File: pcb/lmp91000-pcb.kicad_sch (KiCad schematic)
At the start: 28 parts, among them J1 TC2030, SW1 SW_Push, U1 EFR32BG24L210F768IM40-B, U5 2450AT18D0100001E, Y1 XTL501250-S315-038

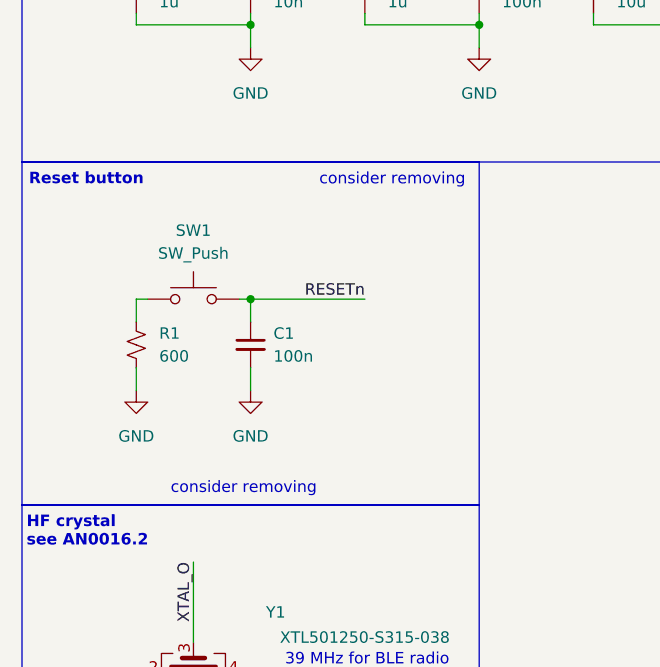
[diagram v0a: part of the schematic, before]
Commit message: Remove reset button
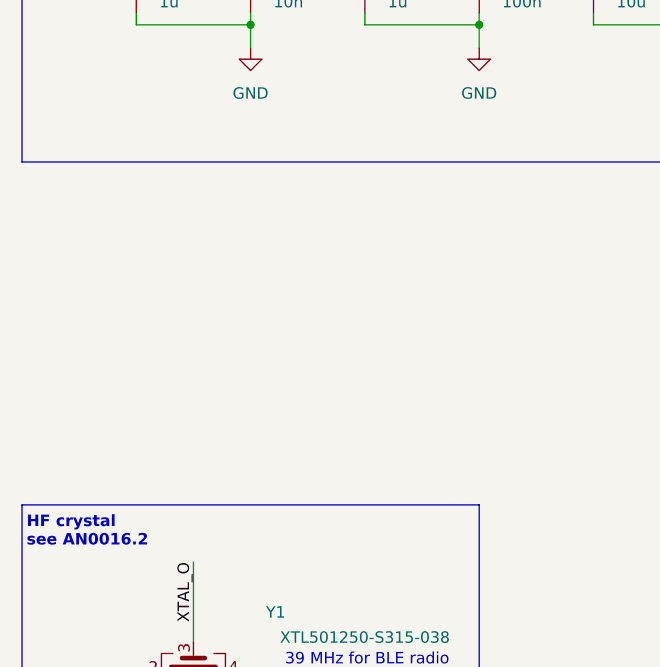
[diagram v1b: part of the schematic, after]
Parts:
- removed C1: 100n, symbol Device:C_Small
- removed R1: 600, symbol Device:R_Small_US
- removed SW1: SW_Push, symbol Switch:SW_Push
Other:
- note removed: "Reset button"
- note removed: "consider removing"

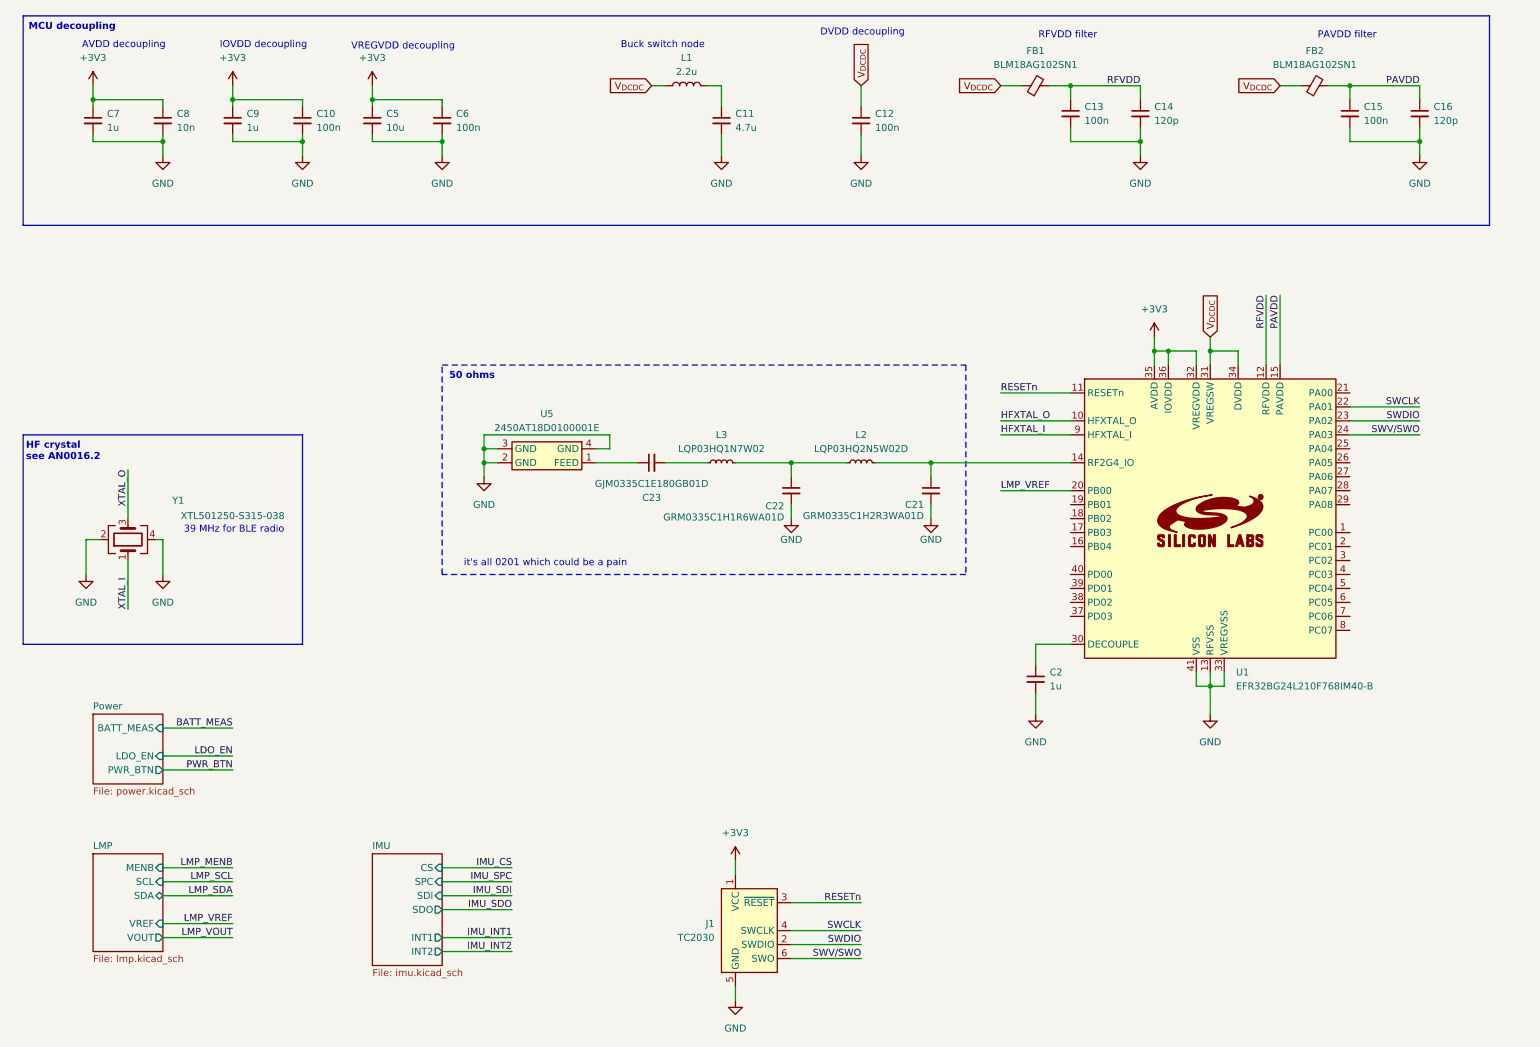
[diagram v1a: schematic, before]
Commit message: Simplify to minimum buck converter components
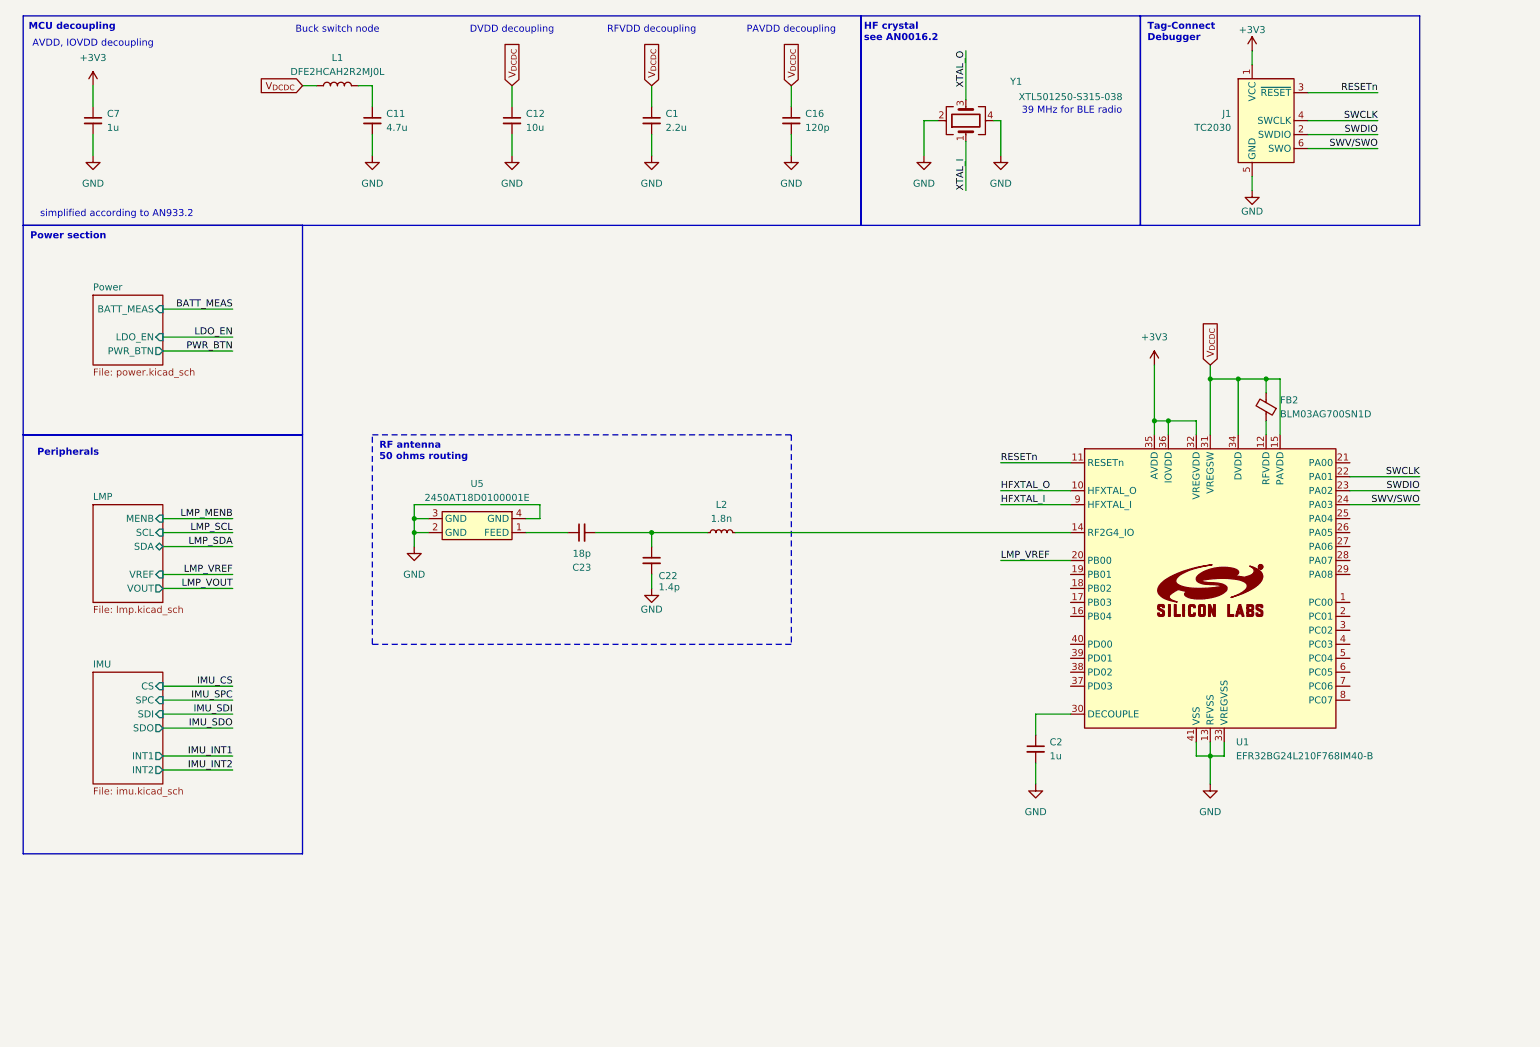
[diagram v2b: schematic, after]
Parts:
- removed C10, C13, C15, C6: 100n, symbol Device:C_Small
- removed C14: 120p, symbol Device:C_Small
- removed C21: GRM0335C1H2R3WA01D, symbol Device:C_Small
- removed C5: 10u, symbol Device:C_Small
- removed C8: 10n, symbol Device:C_Small
- removed C9: 1u, symbol Device:C_Small
- removed FB1: BLM18AG102SN1, symbol Device:FerriteBead_Small
- removed L3: LQP03HQ1N7W02, symbol Device:L_Small
- added C1: 2.2u, symbol Device:C_Small
- C12: value 100n -> 10u
- C22: value GRM0335C1H1R6WA01D -> 1.4p
- C23: value GJM0335C1E180GB01D -> 18p
- FB2: value BLM18AG102SN1 -> BLM03AG700SN1D
- L1: value 2.2u -> DFE2HCAH2R2MJ0L; footprint (none) -> Inductor_SMD:L_1008_2520Metric
- L2: value LQP03HQ2N5W02D -> 1.8n
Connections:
- net PAVDD is gone; now on net V_{DCDC}: C16.1, FB2.2, U1.15 (PAVDD)
- net GND: now also C1.2
- net V_{DCDC}: now also C1.1; no longer FB2.1
- net at C23.2: now also C22.1, L2.1
- net RFVDD: no longer names the net of U1.12 (RFVDD)
- net RFVDD: now also FB2.1
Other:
- note added: "AVDD, IOVDD decoupling"
- note added: "PAVDD decoupling"
- note added: "Peripherals"
- note added: "Power section"
- note added: "RF antenna 50 ohms routing"
- note added: "RFVDD decoupling"
- note added: "Tag-Connect Debugger"
- note added: "simplified according to AN933.2"
- note removed: "50 ohms"
- note removed: "AVDD decoupling"
- note removed: "IOVDD decoupling"
- note removed: "PAVDD filter"
- note removed: "RFVDD filter"
- note removed: "VREGVDD decoupling"
- note removed: "it's all 0201 which could be a pain"
- title: (none) -> LMP91000 Portable Potentiostat
- moved on the sheet: C11, C12, C16, C2, C22, C23, J1, L1, L2, U1, U5, Y1

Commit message: Assign footprints, cleanup schematics, start layout
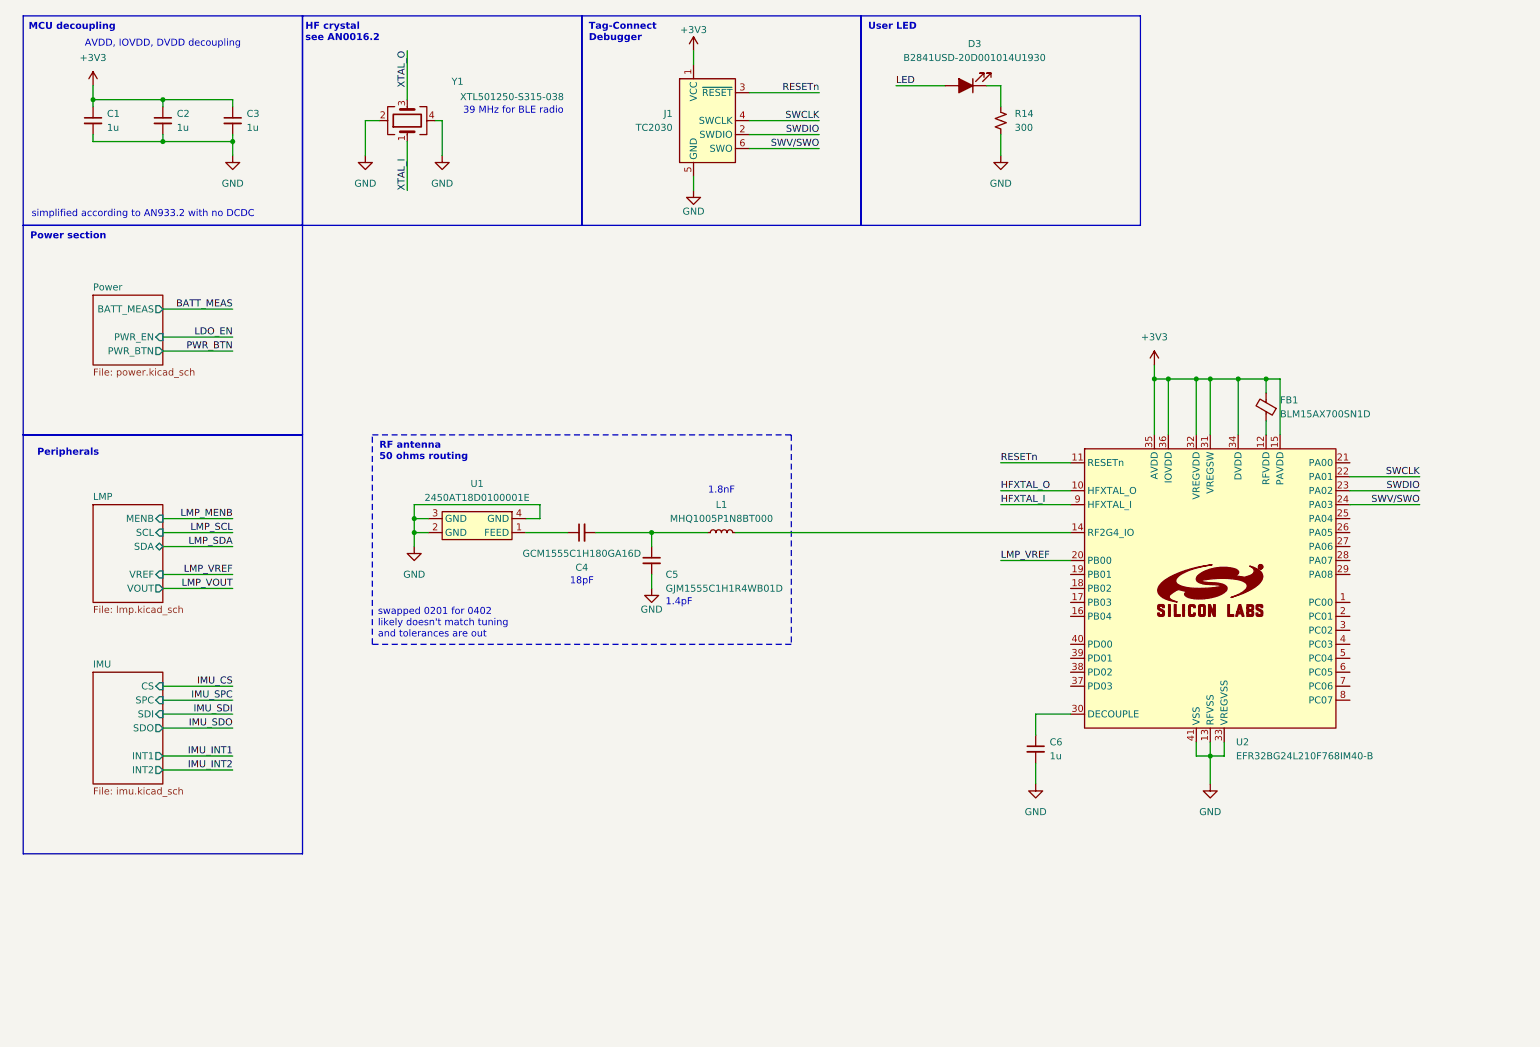
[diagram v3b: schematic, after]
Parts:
- removed C1: 2.2u, symbol Device:C_Small
- removed C11: 4.7u, symbol Device:C_Small
- removed C12: 10u, symbol Device:C_Small
- removed C16: 120p, symbol Device:C_Small
- removed L1: DFE2HCAH2R2MJ0L, Inductor_SMD:L_1008_2520Metric, symbol Device:L
- added C2, C3: 1u, Capacitor_SMD:C_0402_1005Metric, symbol Device:C_Small
- added D3: B2841USD-20D001014U1930, LED_SMD:LED_0402_1005Metric, symbol Device:LED_Filled
- added R14: 300, Resistor_SMD:R_0402_1005Metric, symbol Device:R_Small_US
- C1: renamed from C7; footprint (none) -> Capacitor_SMD:C_0402_1005Metric
- C4: renamed from C23; value 18p -> GCM1555C1H180GA16D; footprint (none) -> Capacitor_SMD:C_0402_1005Metric
- C5: renamed from C22; value 1.4p -> GJM1555C1H1R4WB01D; footprint (none) -> Capacitor_SMD:C_0402_1005Metric
- C6: renamed from C2; footprint (none) -> Capacitor_SMD:C_0402_1005Metric
- FB1: renamed from FB2; value BLM03AG700SN1D -> BLM15AX700SN1D; footprint (none) -> Inductor_SMD:L_0402_1005Metric
- L1: renamed from L2; value 1.8n -> MHQ1005P1N8BT000; footprint (none) -> Inductor_SMD:L_0402_1005Metric
- renumbered U5 to U1, U1 to U2
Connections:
- net V_{DCDC} is gone; now on net +3V3: FB1.2, U2.15 (PAVDD), U2.31 (VREGSW), U2.34 (DVDD)
- net +3V3: now also C2.1, C3.1
- net GND: now also C2.2, C3.2, R14.2
- new net: D3.1 (K), R14.1
- new net LED: D3.2 (A)
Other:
- sheet Power ports: added PWR_EN; removed LDO_EN
- note added: "1.4pF"
- note added: "1.8nF"
- note added: "18pF"
- note added: "AVDD, IOVDD, DVDD decoupling"
- note added: "User LED"
- note added: "simplified according to AN933.2 with no DCDC"
- note added: "swapped 0201 for 0402 likely doesn't match tuning and tolerances are out"
- note removed: "AVDD, IOVDD decoupling"
- note removed: "Buck switch node"
- note removed: "DVDD decoupling"
- note removed: "PAVDD decoupling"
- note removed: "RFVDD decoupling"
- note removed: "simplified according to AN933.2"
- company: (none) -> Clarkson University
- moved on the sheet: J1, Y1

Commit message: Finish PCB
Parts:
- removed C3: 1u, Capacitor_SMD:C_0402_1005Metric, symbol Device:C_Small
- added H1, H2, H3, H4: M2, MountingHole:MountingHole_2.2mm_M2, symbol Mechanical:MountingHole
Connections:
- net XTAL_I is gone; now on net HFXTAL_I: Y1.1
- net XTAL_O is gone; now on net HFXTAL_O: Y1.3
- net BATT_MEAS: now also U2.40 (PD00)
- net IMU_CS: now also U2.7 (PC06)
- net IMU_INT2: now also U2.8 (PC07)
- net IMU_SDI: now also U2.5 (PC04)
- net IMU_SDO: now also U2.4 (PC03)
- net IMU_SPC: now also U2.6 (PC05)
- net LDO_EN: now also U2.1 (PC00)
- net LED: now also U2.29 (PA08)
- net LMP_MENB: now also U2.27 (PA06)
- net LMP_SCL: now also U2.26 (PA05)
- net LMP_SDA: now also U2.25 (PA04)
- net LMP_VOUT: now also U2.21 (PA00)
- net PWR_BTN: now also U2.2 (PC01)
- net FEED: now reaches C4.1, U1.1 (FEED)
- net PI: now reaches C4.2, C5.1, L1.1
- net RF2G4_IO: now reaches L1.2, U2.14 (RF2G4_IO)
- no-connect marks 0 -> 1
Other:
- note added: "AVDD decoupling"
- note added: "Mounting holes"
- note removed: "AVDD, IOVDD, DVDD decoupling"
- note removed: "MCU decoupling"

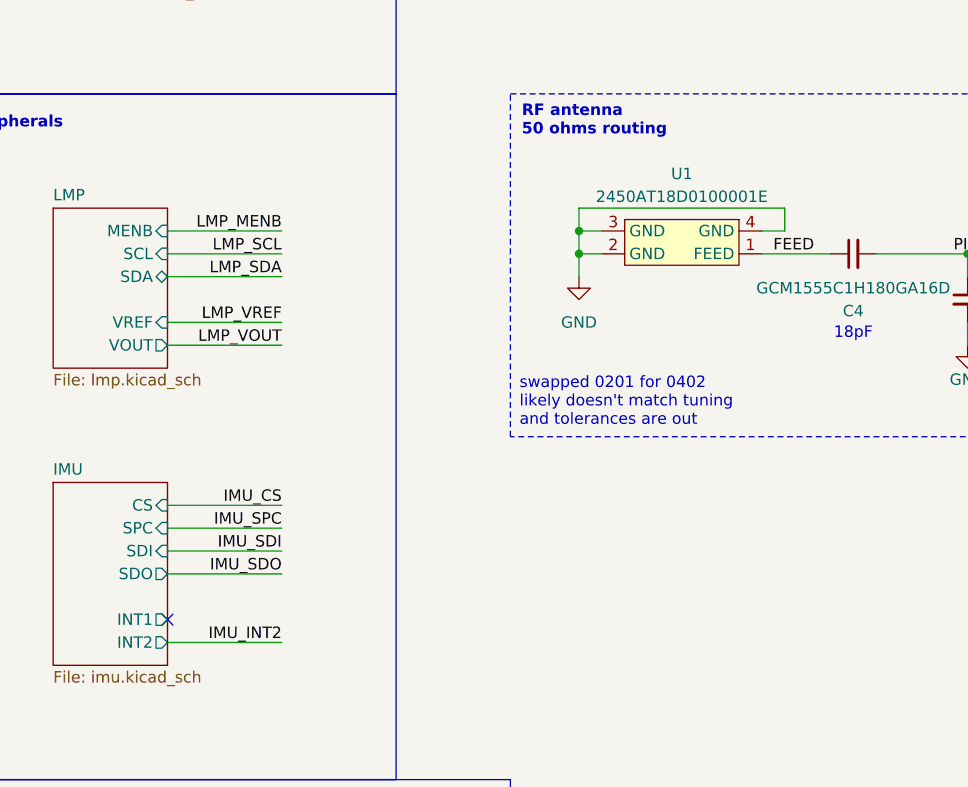
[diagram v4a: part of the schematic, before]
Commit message: Move antenna and tag connect
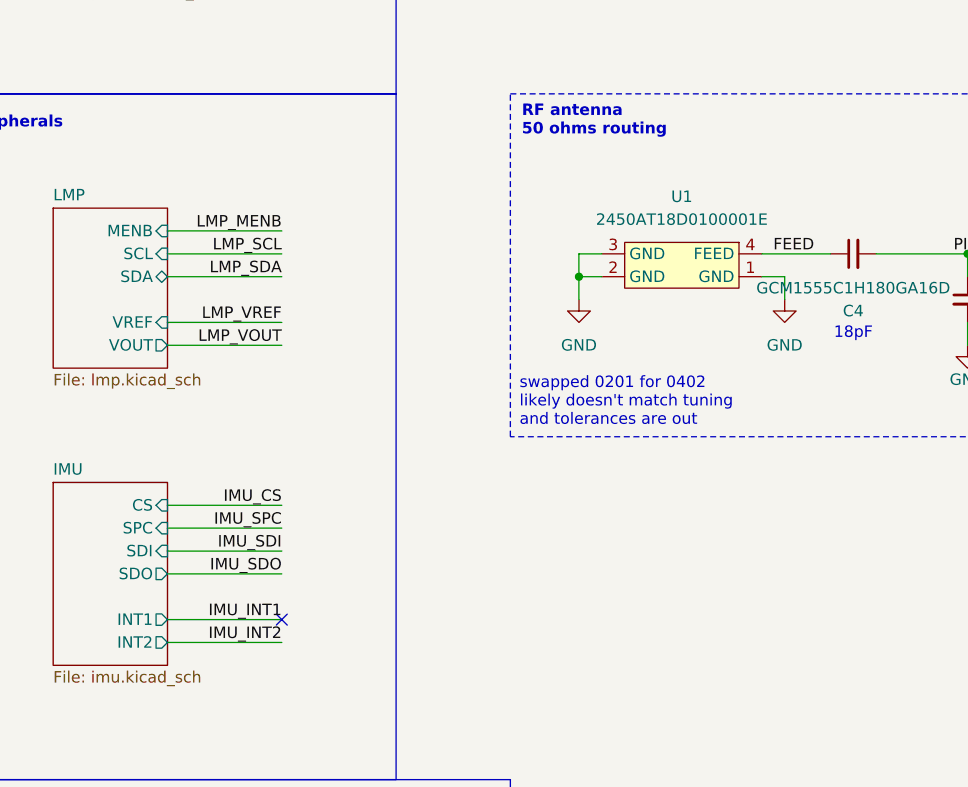
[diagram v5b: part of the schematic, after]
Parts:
- C1, C2, C6: HQ_MPN (none) -> CL05X105KP5NNNC
- C4: HQ_MPN (none) -> CC0402FRNPO9BN180
- C5: HQ_MPN (none) -> GJM1555C1H1R4WB01D
- D3: HQ_MPN (none) -> F.0402.00003/P2-0402R1TS2-045T-001
- FB1: HQ_MPN (none) -> BLM15AX700SN1D
- L1: HQ_MPN (none) -> MHQ1005P1N5BT000
- R14: HQ_MPN (none) -> RTT02301JTH
- U1: HQ_MPN (none) -> 2450AT18D0100001E
- U2: HQ_MPN (none) -> EFR32BG24L210F768IM40-B
- Y1: HQ_MPN (none) -> 7D039000I01
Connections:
- net FEED: now also U1.4 (GND); no longer U1.1 (FEED)
- net GND: now also U1.1 (FEED); no longer U1.4 (GND)
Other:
- moved on the sheet: U1
